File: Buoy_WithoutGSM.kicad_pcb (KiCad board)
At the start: 2 copper layers, 44.2 x 125.6 mm, 20 parts, among them J1 Conn_01x02_Female, J2 Conn_01x05_Male, J3 Conn_01x05_Male, J4 Conn_01x05_Male, J6 Conn_VCC_ESP32, U1 Ultimate_GPS, U2 ESP32-DEVKITC-32D, U3 RFM95W_Board, U4 Ethernet-FeatherWing, U5 AZ1117CR-3.3TRG1

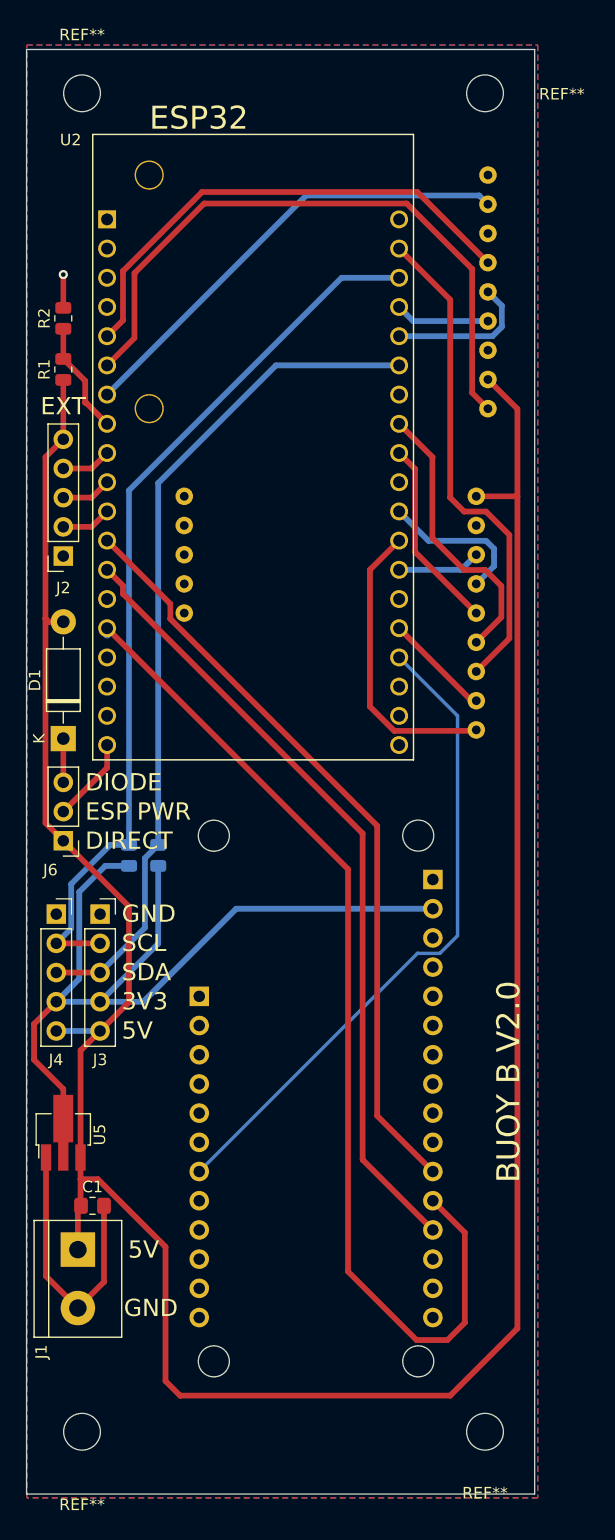
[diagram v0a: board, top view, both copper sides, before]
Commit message: Moved C1 on the PCB, changed PCB shape, moved lower mounting holes
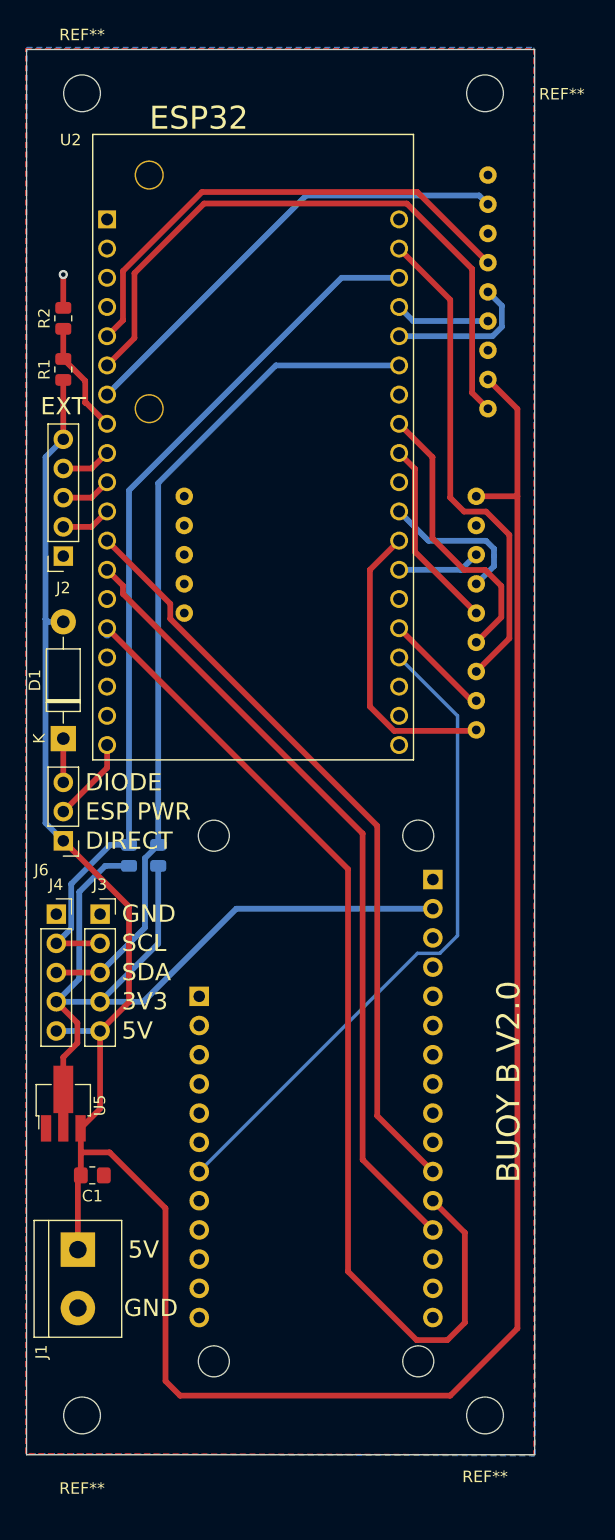
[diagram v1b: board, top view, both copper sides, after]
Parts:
- moved C1 2.65 mm to (132.7, 130.7)
- moved U5 2.54 mm to (130.2, 124.5)
- moved REF** 1.42 mm to (131.8, 151.6)
- moved REF** 1.42 mm to (166.9, 151.6)
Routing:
- net GND: track 27.0 -> 2.90 mm
- net 3V3: track 81.0 -> 77.9 mm
- net 5V: track 228.9 -> 231.8 mm
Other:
- board size 44.2 x 125.6 mm -> 44.2 x 122.2 mm
